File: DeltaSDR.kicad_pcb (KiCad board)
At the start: 2 copper layers, 100 x 80 mm, 179 parts, among them J1 Conn_01x03_Male, J2 Conn_01x05_Male, J3 Barrel_Jack, J4 USB_A, J5 Conn_Coaxial, J6 Conn_01x02_Male, Q1 BSS123, Q2 BSS123, Q3 BSS123, Q4 BSS123, Q5 BSS123, Q6 BSS123, Q7 MMBT3904, T1 Transformer_1P_SS, T2 Transformer_1P_SS, U1 TC1262-33, U10 TLV2464CD, U11 SN74CBT3253, U12 MMG3H21NT1, U2 Si570, U3 SN74CBT3253, U4 PCM3060, U5 CY8C3246PVI-147, U6 TC1262-5, U7 TC1262-5, U8 74HC74, U9 LT6231CSB, Y1 Crystal_GND24

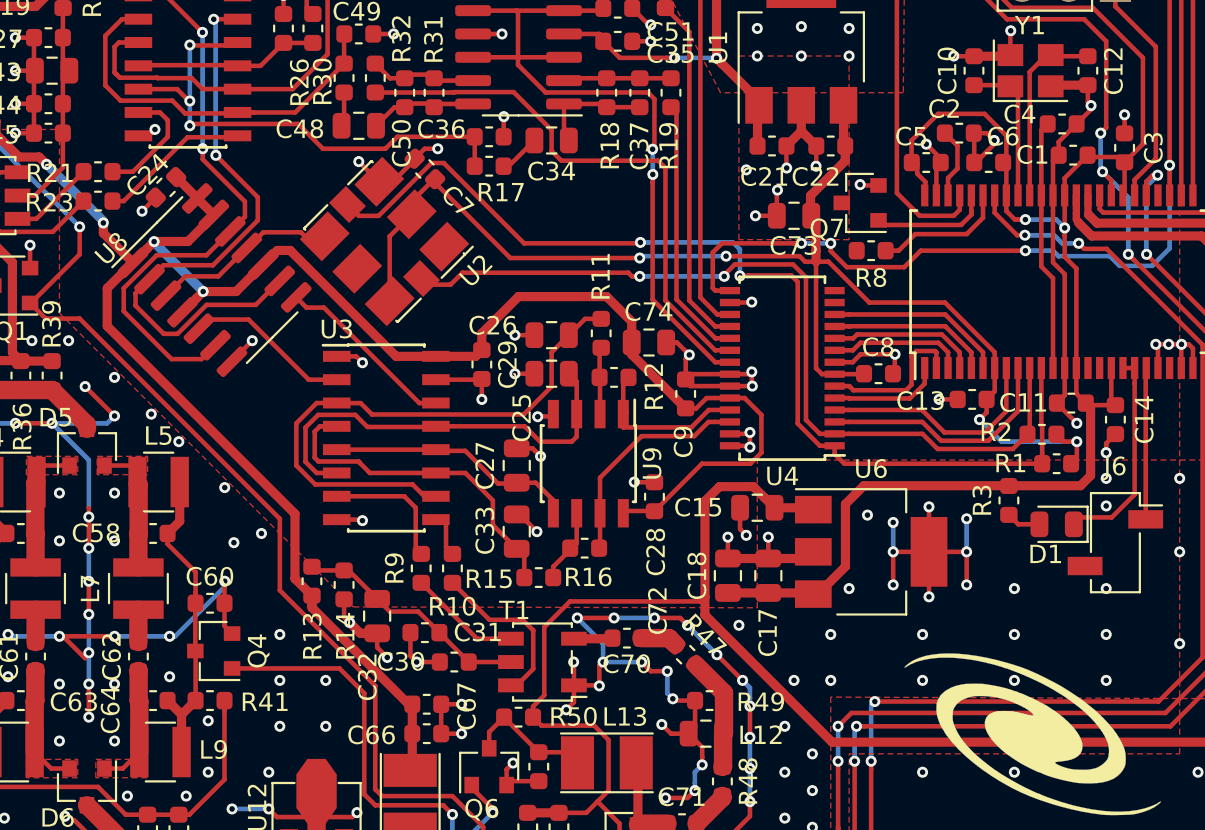
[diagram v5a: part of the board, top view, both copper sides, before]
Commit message: Changed layout of LT6231, changed RX transformer caps ground.
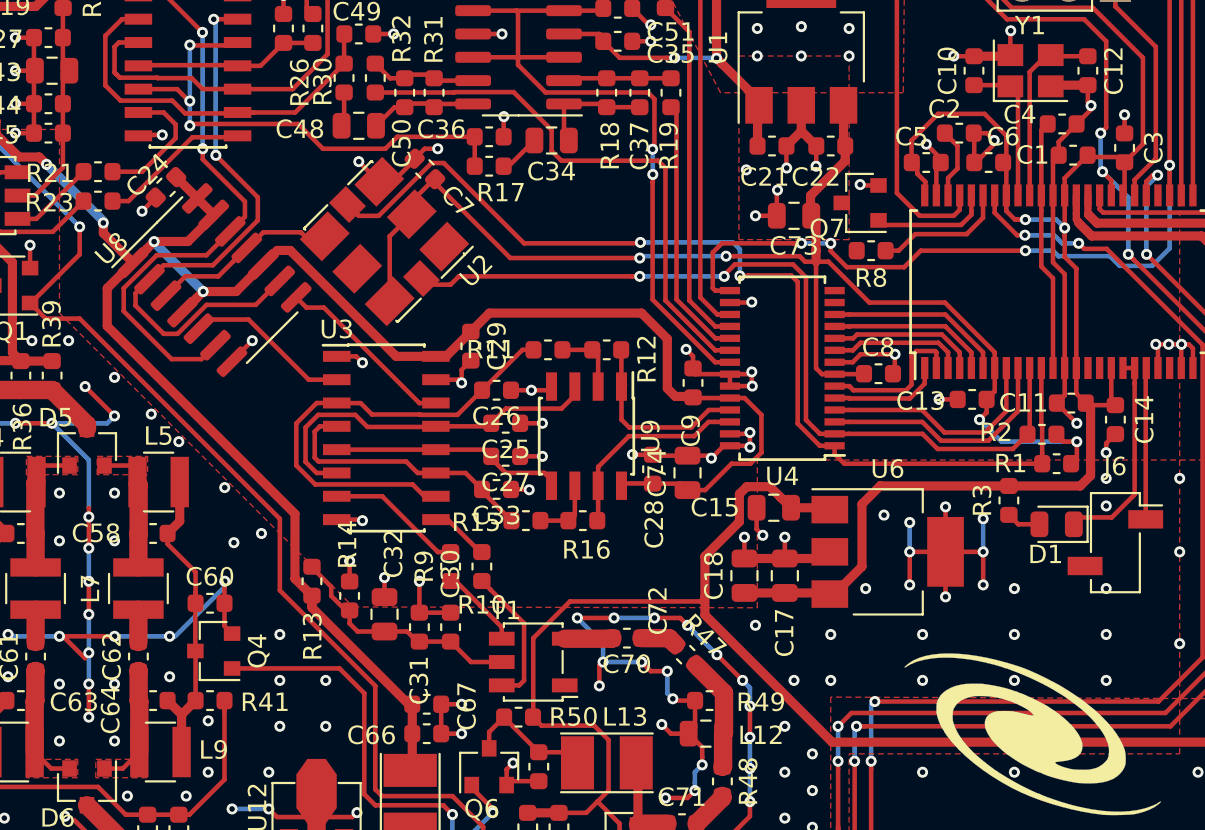
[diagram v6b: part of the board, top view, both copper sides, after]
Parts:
- C25, C26, C27, C33: footprint Capacitor_SMD:C_0805_2012Metric -> Capacitor_SMD:C_0603_1608Metric
- moved C74 7.40 mm to (167.2, 103.7), turned to 90 degrees
- moved C26 4.24 mm to (156.8, 99.2), turned to 180 degrees
- moved C25 3.68 mm to (157.3, 101.0), turned to 180 degrees
- moved R15 3.18 mm to (158.4, 106.3)
- moved R11 3.04 mm to (159.6, 97.0), turned to 0 degrees
- moved C33 2.55 mm to (156.8, 104.6), turned to 180 degrees
- moved C30 1.91 mm to (154.3, 112.1), turned to 90 degrees
- moved R9 1.60 mm to (154.3, 108.8)
- moved R10 1.60 mm to (156.0, 108.8)
- moved R12 1.55 mm to (162.8, 97.0)
- moved U9 1.50 mm to (161.7, 101.7)
- moved C28 1.50 mm to (165.3, 103.5)
- moved R16 1.50 mm to (161.5, 106.3)
- moved C29 1.17 mm to (155.4, 96.8)
- moved C15 0.90 mm to (171.9, 105.6)
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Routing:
- net GND: track 513.1 -> 507.4 mm, vias 524 -> 522
- net Net-(C26-Pad2): track 31.7 -> 26.2 mm
- net Net-(C33-Pad2): track 17.9 -> 14.4 mm
- net Net-(C25-Pad2): track 22.7 -> 20.2 mm
- net Net-(R9-Pad1): track 6.15 -> 4.46 mm
- net VINL: track 9.32 -> 10.8 mm
- net Net-(R10-Pad1): track 9.15 -> 7.69 mm
- net Net-(R10-Pad2): track 2.01 -> 3.23 mm
- net VINR: track 12.2 -> 11.3 mm
- net +5VD: track 90.5 -> 89.6 mm
- net Net-(R15-Pad2): track 4.15 -> 3.28 mm
- net Net-(R21-Pad2): track 7.03 -> 7.79 mm
- net +5V: track 191.3 -> 190.6 mm
- net Net-(R9-Pad2): track 7.75 -> 8.36 mm
- net RX_RF: track 2.11 -> 2.61 mm

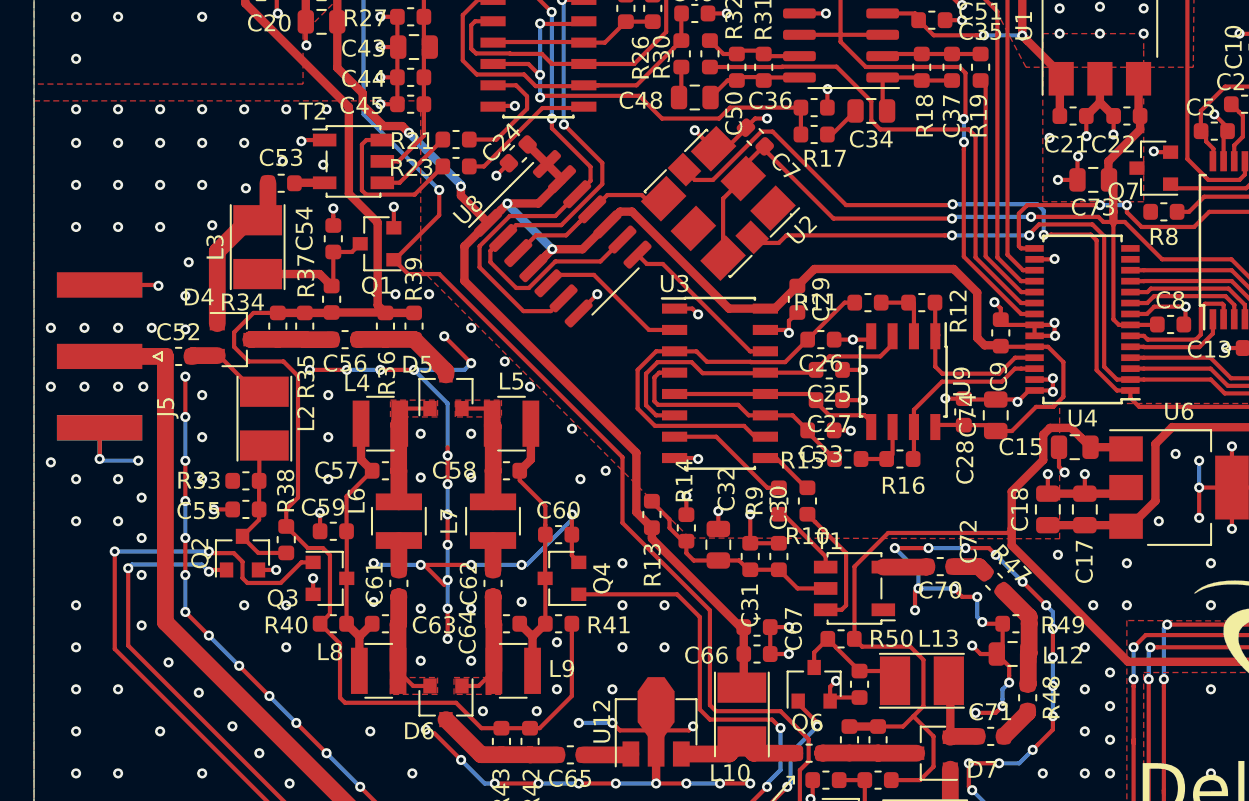
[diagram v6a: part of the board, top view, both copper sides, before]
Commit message: Improved layout of band pass switches, edited README.md
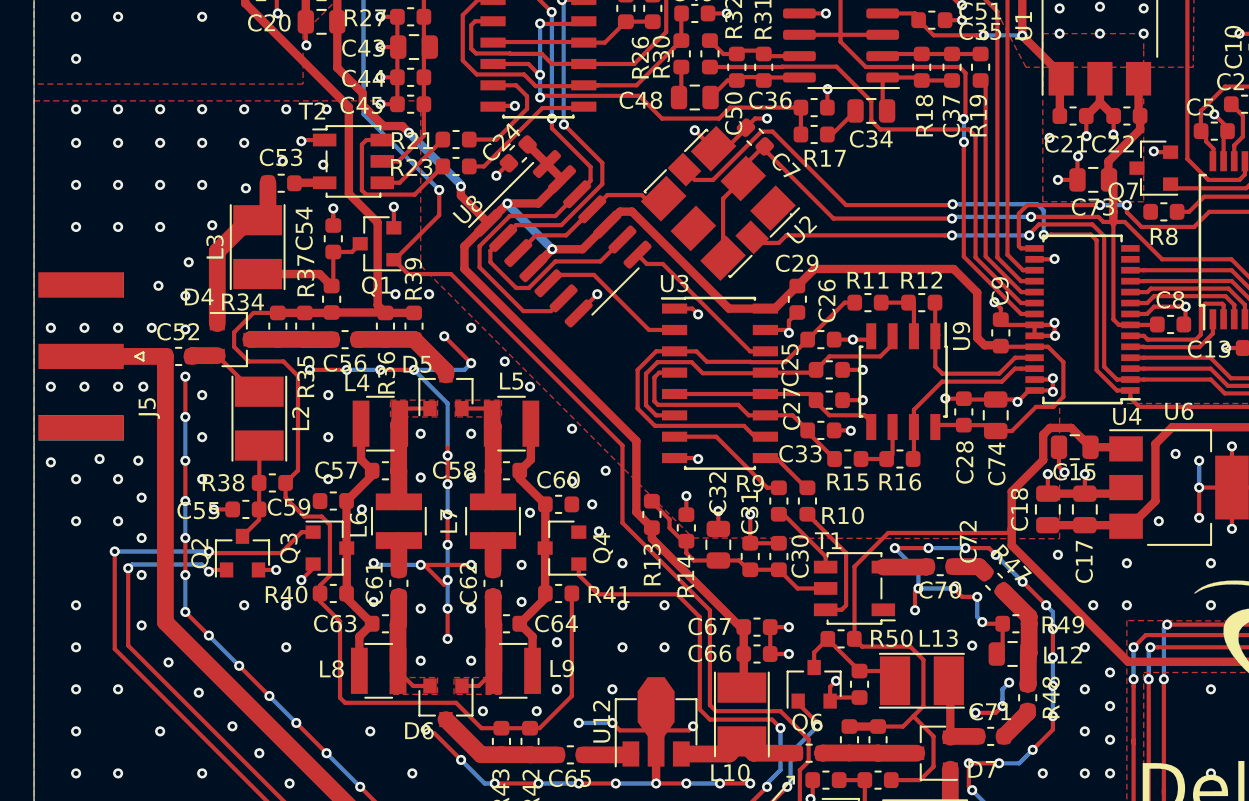
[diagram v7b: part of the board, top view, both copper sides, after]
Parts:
- removed R33: 2k2, Resistor_SMD:R_0603_1608Metric
- moved R38 3.47 mm to (124.2, 107.7), turned to 180 degrees
- moved Q3 1.80 mm to (127.6, 111.6)
- moved Q4 1.80 mm to (141.4, 111.6)
- moved C59 1.80 mm to (127.8, 108.8)
- moved C60 1.80 mm to (141.2, 109.0)
- moved R40 1.80 mm to (127.8, 114.3)
- moved R41 1.80 mm to (141.2, 114.3)
- moved J5 1.10 mm to (112.8, 100.2)
- moved L2 0.30 mm to (123.4, 103.9)
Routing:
- net GND: track 507.4 -> 483.1 mm, vias 522 -> 524
- net Net-(C55-Pad2): track 8.85 -> 5.81 mm
- net +12V: track 302.4 -> 304.3 mm
- net B6040M: track 157.1 -> 155.8 mm
- net B80M: track 126.6 -> 127.7 mm

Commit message: Changed LDOs
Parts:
- C15, C23: value 10u -> 1u
- U1: value TC1262-33 -> MCP1703T-3302E/DB
- U6, U7: value TC1262-5 -> MCP1703T-5002E/DB
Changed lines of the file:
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@@
       (effects (font (size 1 1) (thickness 0.15)))
     )
-    (fp_text value TC1262-33 (at 0 4.5 90) (layer F.Fab)
+    (fp_text value MCP1703T-3302E/DB (at 0 4.5 90) (layer F.Fab)
       (effects (font (size 1 1) (thickness 0.15)))
     )
@@
       (effects (font (size 1 1) (thickness 0.15)))
     )
-    (fp_text value TC1262-5 (at 0 4.5 90) (layer F.Fab)
+    (fp_text value MCP1703T-5002E/DB (at 0 4.5 90) (layer F.Fab)
       (effects (font (size 1 1) (thickness 0.15)))
     )
@@
       (effects (font (size 1 1) (thickness 0.15)))
     )
-    (fp_text value TC1262-5 (at 0 4.5) (layer F.Fab)
+    (fp_text value MCP1703T-5002E/DB (at 0 4.5) (layer F.Fab)
       (effects (font (size 1 1) (thickness 0.15)))
     )
@@
       (effects (font (size 1 1) (thickness 0.15)))
     )
-    (fp_text value 10u (at 0 1.65) (layer F.Fab)
+    (fp_text value 1u (at 0 1.65) (layer F.Fab)
       (effects (font (size 1 1) (thickness 0.15)))
     )
@@
       (effects (font (size 1 1) (thickness 0.15)))
     )
-    (fp_text value 10u (at 0 1.65) (layer F.Fab)
+    (fp_text value 1u (at 0 1.65) (layer F.Fab)
       (effects (font (size 1 1) (thickness 0.15)))
     )
